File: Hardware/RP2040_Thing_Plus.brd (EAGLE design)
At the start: 22.9 x 58.4 mm, 67 parts, among them J5 USB Female Type C Connector, J6 MICRO-SD-SDIOPUSH-PUSH, Q1 2.5A/30V, U1 MCP73831, U2 MAX17048, U3 AP2112K-3.3V, U4 W25QXX128MBIT, U5 RP2040, Y2 12MHz

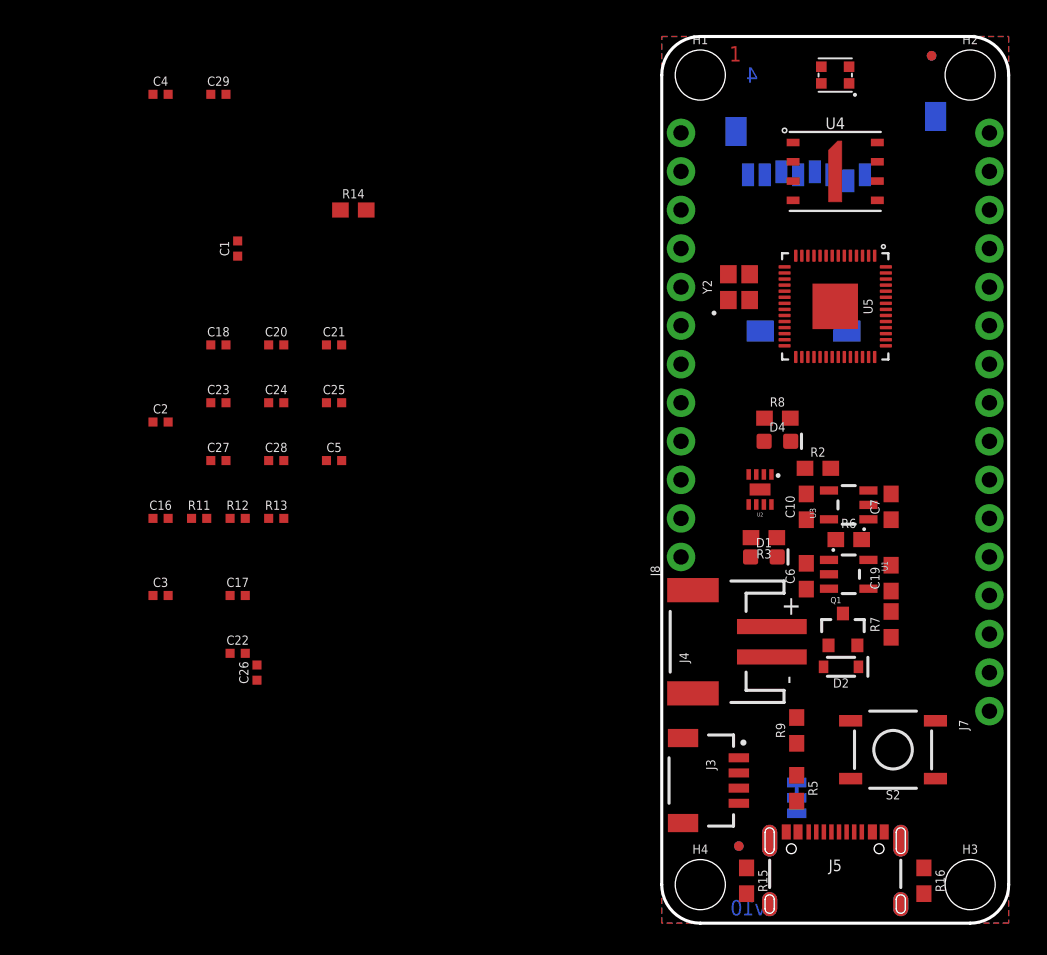
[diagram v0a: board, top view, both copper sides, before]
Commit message: airwire corrections
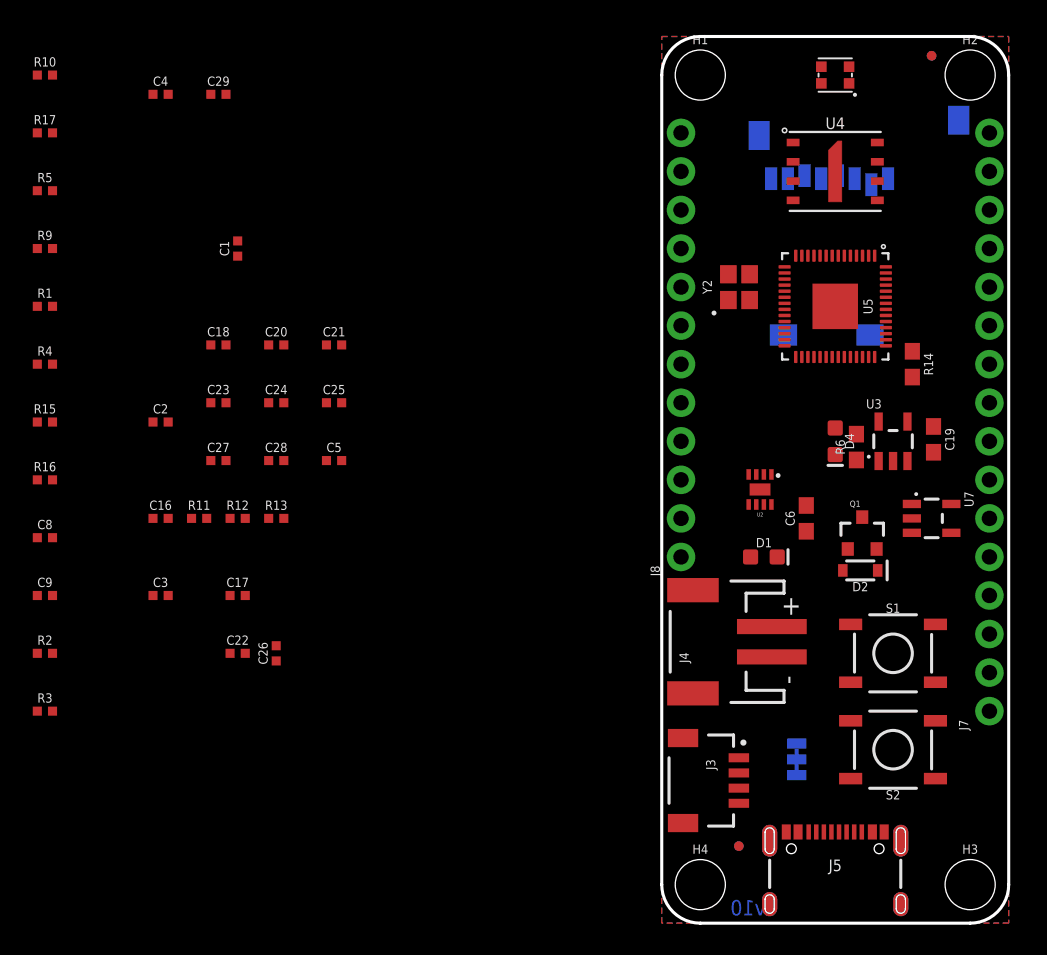
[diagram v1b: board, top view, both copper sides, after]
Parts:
- removed C10: 2.2uF, SparkFun-Capacitors:0603
- removed C7: 1.0uF, SparkFun-Capacitors:0603@1
- removed R7: 10k, SparkFun-Resistors:0603
- removed R8: 330, SparkFun-Resistors:0603
- removed U1: MCP73831, SparkFun-PowerIC:SOT23-5
- added C8: 1.0uF, SparkFun-Capacitors:0402-TIGHT
- added C9: 2.2uF, SparkFun-Capacitors:0402-TIGHT
- added R1, R4: 5.1k, SparkFun-Resistors:0402-TIGHT
- added R10, R17: 2.2k, SparkFun-Resistors:0402-TIGHT
- added S1: MOMENTARY-SWITCH-SPST-SMD-5.2MM-TALL, SparkFun-Switches:TACTILE_SWITCH_SMD_5.2MM
- added U7: 3.3V, SparkFun-IC-Power:SOT23-5
- C19, C6: device SparkFun-Capacitors:0603@1 -> SparkFun-Capacitors:0603
- J3: value (none) -> QWIIC_RIGHT_ANGLE
- R15, R16: value 5.1k -> 10k; device SparkFun-Resistors:0603 -> SparkFun-Resistors:0402-TIGHT
- R2: value 10k -> 1k; device SparkFun-Resistors:0603 -> SparkFun-Resistors:0402-TIGHT
- R3: value 1K -> 1k; device SparkFun-Resistors:0603 -> SparkFun-Resistors:0402-TIGHT
- R5: value 2.2k -> 1k; device SparkFun-Resistors:0603 -> SparkFun-Resistors:0402-TIGHT
- R9: value 2.2k -> 10k; device SparkFun-Resistors:0603 -> SparkFun-Resistors:0402-TIGHT
- U3: value AP2112K-3.3V -> MCP73831; device SparkFun-PowerIC:SOT23-5 -> SparkFun-IC-Power:SOT23-5
- moved R16 63.7 mm to (-40.6, 29.2), turned to 0 degrees
- moved R5 63.3 mm to (-40.6, 48.3), turned to 0 degrees
- moved R9 58.8 mm to (-40.6, 44.5), turned to 0 degrees
- moved R15 55.2 mm to (-40.6, 33.0), turned to 0 degrees
- moved R2 52.4 mm to (-40.6, 17.8)
- moved R3 48.7 mm to (-40.6, 14.0), turned to 0 degrees
- moved R14 38.2 mm to (16.5, 36.8), turned to 270 degrees
- moved C19 9.56 mm to (17.9, 31.9), turned to 270 degrees
- moved D2 6.48 mm to (13.1, 23.2)
- moved Q1 6.48 mm to (13.2, 25.7)
- moved R6 6.12 mm to (12.8, 31.4), turned to 90 degrees
- moved U3 5.11 mm to (15.2, 31.8), turned to 0 degrees
- moved C6 3.81 mm to (9.53, 26.7)
- moved D4 3.81 mm to (11.4, 31.8), turned to 270 degrees
- moved U$68 2.54 mm to (6.10, 11.6)
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- renumbered U$3 to U6
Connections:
- removed net D13: D4.A
- removed net VIN: C7.1, D2.C, Q1.2, R2.2, U3.1
- new net BOOT: R5.2, S1.3
- new net N$15: C8.1, D2.C, Q1.2, R16.2, U7.1
- net 3.3V: now also C9.1, R9.2, U7.5; no longer C10.1, U3.5
- net EN: now also R16.1, U7.3; no longer R2.1, U3.3
- net GND: now also C8.2, C9.2, R1.2, R15.1, R3.1, R4.2, S1.1, U7.2; no longer C10.2, C7.2, R15.2, R16.2, R7.1, R8.1, U1.2
- net I2C1_SCL: now also R10.1; no longer R5.1
- net I2C1_SDA: now also R17.1; no longer R9.1
- net LED_BUILTIN: now also D4.A
- net N$1: now also R3.2; no longer R8.2
- net N$11: now also R1.1; no longer R15.1
- net N$12: now also R4.1; no longer R16.1
- net N$14: now also U3.5; no longer U1.5
- net N$17: now also R2.1; no longer R3.2
- net N$2: now also R10.2; no longer R5.2
- net N$3: now also R17.2; no longer R9.2
- net N$9: now also U3.1; no longer U1.1
- net QSPI-CS: now also R5.1, R9.1
- net V_BATT: now also U3.3; no longer U1.3
- net V_USB: now also R15.2, R2.2, U3.4; no longer R3.1, R7.2, U1.4
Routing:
- net I2C1_SCL: track 35.2 -> 0.00 mm
- net I2C1_SDA: track 32.3 -> 0.00 mm
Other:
- board text removed: "1"
- board text removed: "2"
- board text removed: "3"
- board text removed: "4"

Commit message: v01 review
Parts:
- removed C19, C6: 4.7uF, SparkFun-Capacitors:0603
- removed R14: 200, SparkFun-Resistors:0603
- removed U$67: (no value), buzzard_labels (39):I_C0
- removed U$68: (no value), buzzard_labels (39):21
- added C10, C7: 4.7uF, SparkFun-Capacitors:0402-TIGHT
- added J1: CORTEX_JTAG_DEBUG_MINIMUM_PTH, SparkFun-Connectors:2X5-PTH-1.27MM
- added R7: 200OHM-0402T-1/16W-1%, SparkFun-Resistors:0402-TIGHT
- added U$1, U$39: (no value), output:#_16#0
- added U$10: (no value), output:#WS2812_#0
- added U$11: (no value), output:#0#TX_#0
- added U$12: (no value), output:#1#RX_#0
- added U$13: (no value), output:#4#CIPO_#0
- added U$14: (no value), output:#3#COPI_#0
- added U$15: (no value), output:#2#SCK_#0
- added U$16, U$17, U$51, U$52: (no value), output:#NC_#0
- added U$18, U$50: (no value), output:#29#ADC3_#0
- added U$19, U$49: (no value), output:#28#ADC2_#0
- added U$2, U$38: (no value), output:#_17#0
- added U$20, U$48: (no value), output:#27#ADC1_#0
- added U$21, U$47: (no value), output:#26#ADC0_#0
- added U$22, U$40: (no value), output:#_VUSB#0
- added U$23, U$41: (no value), output:#_EN#0
- added U$24, U$42: (no value), output:#_VBATT#0
- added U$25, U$46: (no value), output:#GND_#0
- added U$26, U$45: (no value), output:#AREF_#0
- added U$27, U$44: (no value), output:#3#3V_#0
- added U$28, U$43: (no value), output:##RESET##0
- added U$29, U$9: (no value), output:#_SDA#6#0
- added U$3, U$37: (no value), output:#_18#0
- added U$30: (no value), Labels:I_SUPER2_C-()-03
- added U$32: (no value), SparkFun-Aesthetics:SFE_LOGO_NAME_FLAME_.1
- added U$33, U$7: (no value), output:#_22#0
- added U$34, U$6: (no value), output:#_21#0
- added U$35, U$5: (no value), output:#_20#0
- added U$36, U$4: (no value), output:#_19#0
- added U$53: (no value), output:RP2040_THING_PLUS0
- added U$59: (no value), output:#BOOT#0
- added U$60: (no value), output:#WS2812#0
- added U$61: (no value), output:#25#0
- added U$62: (no value), output:#CHARGE#0
- added U$64: (no value), SparkFun-Aesthetics:QWIIC_4MM
- added U$8: (no value), output:#_SCL#7#23#0
- R6: value 2.0k -> 2.0KOHM-0402T-1/16W-5%; device SparkFun-Resistors:0603 -> SparkFun-Resistors:0402-TIGHT
- moved R10 68.7 mm to (8.26, 7.62), flipped to the bottom, turned to 180 degrees
- moved R4 66.5 mm to (16.9, 3.43), turned to 90 degrees
- moved R17 63.6 mm to (8.26, 11.4), flipped to the bottom, turned to 180 degrees
- moved R1 59.6 mm to (5.97, 3.56), turned to 90 degrees
- moved R5 59.5 mm to (15.6, 28.8), flipped to the bottom, turned to 180 degrees
- moved R9 58.2 mm to (15.6, 29.7), flipped to the bottom, turned to 180 degrees
- moved R15 58.0 mm to (14.2, 14.2), turned to 180 degrees
- moved C9 55.9 mm to (15.2, 22.6), turned to 180 degrees
- moved C3 54.1 mm to (11.4, 52.5)
- moved R16 53.7 mm to (12.3, 20.1), turned to 90 degrees
- moved C22 53.4 mm to (14.7, 49.9), turned to 90 degrees
- moved R3 53.4 mm to (9.02, 33.5), turned to 270 degrees
- moved C8 53.1 mm to (12.3, 22.1), turned to 90 degrees
- moved R2 52.6 mm to (10.8, 29.0)
- moved C18 48.6 mm to (19.1, 43.6)
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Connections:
- net N$7 renamed USB_F_N
- net N$8 renamed USB_F_P
- removed net D+: J5.A6, J5.B6
- removed net D-: J5.A7, J5.B7
- removed net I2C1_SCL: J3.4, J8.11, R10.1, U2.7, U5.9
- removed net N$10: C28.1, R14.1, U5.43
- removed net N$23: U5.11
- removed net USB_D+: R13.1
- removed net USB_D-: R12.1
- new net AVDD: C28.1, J7.3, R7.1, U5.43
- new net I2C1_SCL/GPIO23: J3.4, J8.11, R10.1, U2.7, U5.35, U5.9
- new net USB_N: J5.A7, J5.B7, R12.1
- new net USB_P: J5.A6, J5.B6, R13.1
- net !RESET: now also J1.10
- net 3.3V: now also J1.1, R7.2; no longer R14.2
- net BATT_ALERT: now also U5.36; no longer U5.7
- net GND: now also C10.2, C7.2, J1.3, J1.5, J1.9; no longer C19.2, C6.2
- net GPIO16: now also J8.4; no longer J8.10
- net GPIO17: now also J8.5; no longer J8.9
- net GPIO18: now also J8.6; no longer J8.8
- net GPIO20: now also J8.8; no longer J8.6
- net GPIO21: now also J8.9; no longer J8.5
- net GPIO22: now also J8.10; no longer J8.4
- net N$13: now also U5.7; no longer U5.35
- net SWDCK: now also J1.4
- net SWDIO: now also J1.2
- net V_BATT: now also C10.1; no longer C6.1
- net V_USB: now also C7.1; no longer C19.1
- net WS2812_DI: now also U5.11; no longer U5.36
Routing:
- net I2C1_SCL/GPIO23: track 0.00 -> 72.6 mm, vias 0 -> 5
- net I2C1_SDA: track 0.00 -> 70.1 mm, vias 0 -> 3
- net 3.3V: track 0.00 -> 53.5 mm, vias 0 -> 15
- net V_USB: track 0.00 -> 43.7 mm, vias 0 -> 4
- net QSPI-0: track 0.00 -> 36.0 mm, vias 0 -> 3
- net USB_N: track 0.00 -> 35.0 mm, vias 0 -> 1
- net V_BATT: track 0.00 -> 35.0 mm, vias 0 -> 2
- net USB_P: track 0.00 -> 34.9 mm, vias 0 -> 1
- net QSPI-3: track 0.00 -> 34.2 mm, vias 0 -> 3
- net QSPI-CLK: track 0.00 -> 34.0 mm, vias 0 -> 3
- net !RESET: track 0.00 -> 33.0 mm, vias 0 -> 1
- net AVDD: track 0.00 -> 30.5 mm, vias 0 -> 1
- net BOOT: track 0.00 -> 27.5 mm, vias 0 -> 3
- net 1.1V: track 0.00 -> 27.0 mm, vias 0 -> 2
- net QSPI-CS: track 0.00 -> 26.2 mm, vias 0 -> 2
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
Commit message: Review Changes
- Add "Pi Thing Plus RP2040" silk
- Align LEDs
- Change LED label style
- Flip bottom silk labels
- Add GND vias
- Beef up power traces
- Add thermal vias under RP2040
- Straighten trace on ADC0
- Add SDA/SCL Labels to bottom silk
- Add PWR LED
- Move QSPI resistors to make room for silk

Passes micromod.dru (overlap errors for jumper footprint + thermal vias)
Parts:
- removed U$46: (no value), output:#GND_#0
- removed U$47: (no value), output:#26#ADC0_#0
- removed U$48: (no value), output:#27#ADC1_#0
- removed U$49: (no value), output:#28#ADC2_#0
- removed U$50: (no value), output:#29#ADC3_#0
- removed U$51, U$52: (no value), output:#NC_#0
- removed U$53: (no value), output:RP2040_THING_PLUS0
- added D3: RED, SparkFun-LED:LED-0603
- added R8: 1k, SparkFun-Resistors:0402-TIGHT
- added U$54: (no value), output:250
- added U$55: (no value), output:CHARGE0
- added U$56: (no value), output:BOOT0
- added U$57: (no value), output:#22_#0
- added U$58: (no value), output:#21_#0
- added U$63: (no value), output:#17_#0
- added U$65: (no value), output:#16_#0
- added U$66: (no value), output:#VUSB_#0
- added U$67: (no value), output:#EN_#0
- added U$68: (no value), output:#VBATT_#0
- added U$69, U$70: (no value), output:#_NC#0
- U$16: device output:#NC_#0 -> output:PWR0
- U$17: device output:#NC_#0 -> output:#I�C#0
- U$29: device output:#_SDA#6#0 -> output:PI_THING_PLUS0
- U$30: device Labels:I_SUPER2_C-()-03 -> output:RP20400
- U$33: device output:#_22#0 -> output:#SCL_#0
- U$34: device output:#_21#0 -> output:#SDA_#0
- U$35: device output:#_20#0 -> output:#_#RESET##0
- U$36: device output:#_19#0 -> output:#_3#3V#0
- U$37: device output:#_18#0 -> output:#_AREF#0
- U$38: device output:#_17#0 -> output:#_GND#0
- U$39: device output:#_16#0 -> output:#_26#ADC0#0
- U$40: device output:#_VUSB#0 -> output:#_27#ADC1#0
- U$41: device output:#_EN#0 -> output:#_28#ADC2#0
- U$42: device output:#_VBATT#0 -> output:#_29#ADC3#0
- U$43: device output:##RESET##0 -> output:PI_THING_PLUS_0
- U$44: device output:#3#3V_#0 -> output:RP2040_0
- U$45: device output:#AREF_#0 -> SparkFun-Aesthetics:SFE_LOGO_NAME_.1
- U$59: device output:#BOOT#0 -> output:#20_#0
- U$61: device output:#25#0 -> output:#19_#0
- U$62: device output:#CHARGE#0 -> output:#18_#0
- moved U$35 34.2 mm to (21.2, 14.0), turned to 0 degrees
- moved U$29 34.0 mm to (8.08, 18.7), flipped to the bottom
- moved U$16 31.7 mm to (18.8, 5.21)
- moved U$36 30.2 mm to (21.2, 16.5), turned to 0 degrees
- moved U$59 29.5 mm to (1.65, 41.9), flipped to the bottom
- moved U$17 28.9 mm to (6.63, 9.53), flipped to the bottom, turned to 90 degrees
- moved U$37 26.5 mm to (21.2, 19.1), turned to 0 degrees
- moved U$38 23.4 mm to (21.2, 21.6), turned to 0 degrees
- moved U$43 21.8 mm to (16.5, 35.3), flipped to the top, turned to 0 degrees
- moved U$39 21.1 mm to (21.2, 24.1), turned to 0 degrees
- moved U$42 21.1 mm to (21.2, 31.8), turned to 0 degrees
- moved U$40 19.8 mm to (21.2, 26.7), turned to 0 degrees
- moved U$41 19.8 mm to (21.2, 29.2), turned to 0 degrees
- moved U$45 18.8 mm to (14.4, 36.6), flipped to the top, turned to 0 degrees
- moved U$44 18.3 mm to (16.6, 34.1), flipped to the top, turned to 0 degrees
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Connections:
- new net N$7: D3.C, R8.2
- net 3.3V: now also D3.A
- net GND: now also R8.1
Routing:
- net N$7: track 0.00 -> 2.43 mm
- net QSPI-CS: track 26.2 -> 24.6 mm
- net BOOT: track 27.5 -> 28.8 mm
- net UART0_RX: track 9.54 -> 10.7 mm
- net V_BATT: track 35.0 -> 35.6 mm
- net N$15: track 9.41 -> 9.95 mm
- net 3.3V: track 53.5 -> 52.9 mm, vias 15 -> 16
- net GND: vias 9 -> 50
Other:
- board text added: "N. Poole"

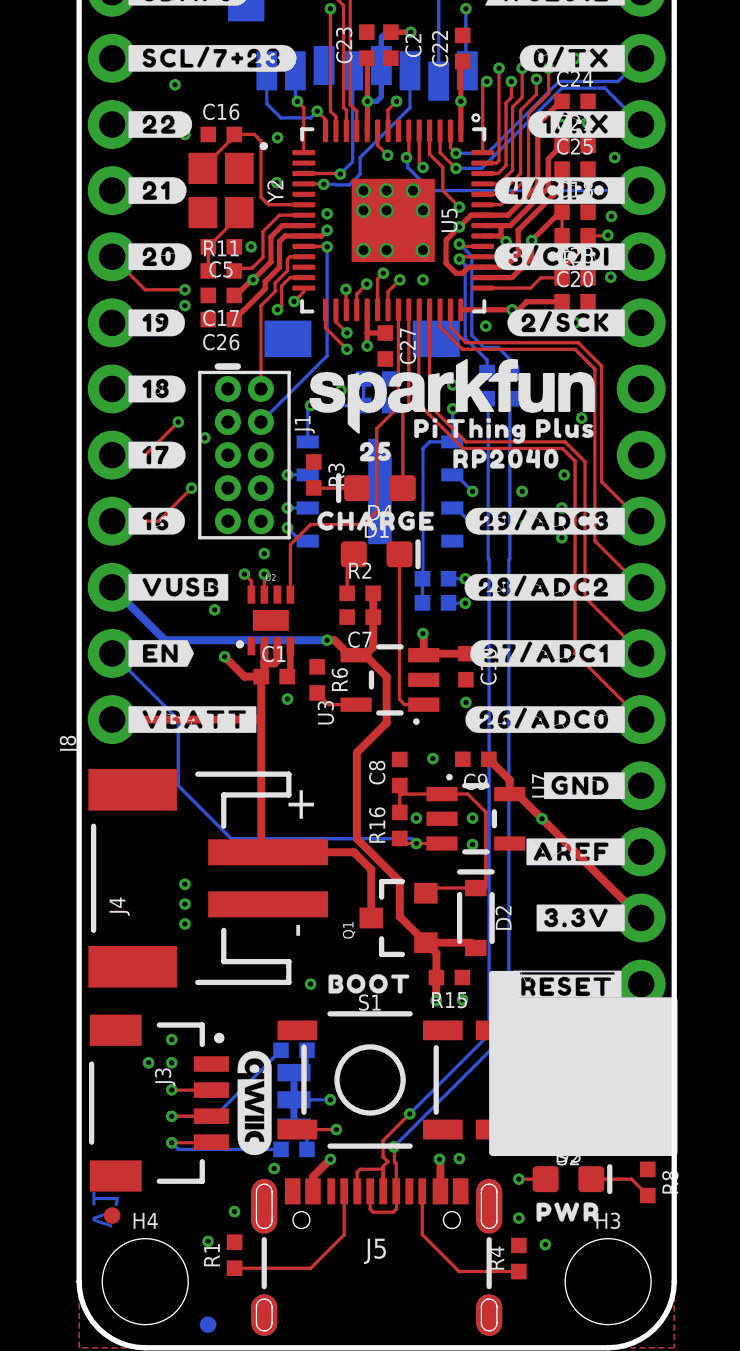
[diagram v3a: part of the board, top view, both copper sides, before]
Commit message: Move silk on LiPo connector. Add ignore. Remove backups.
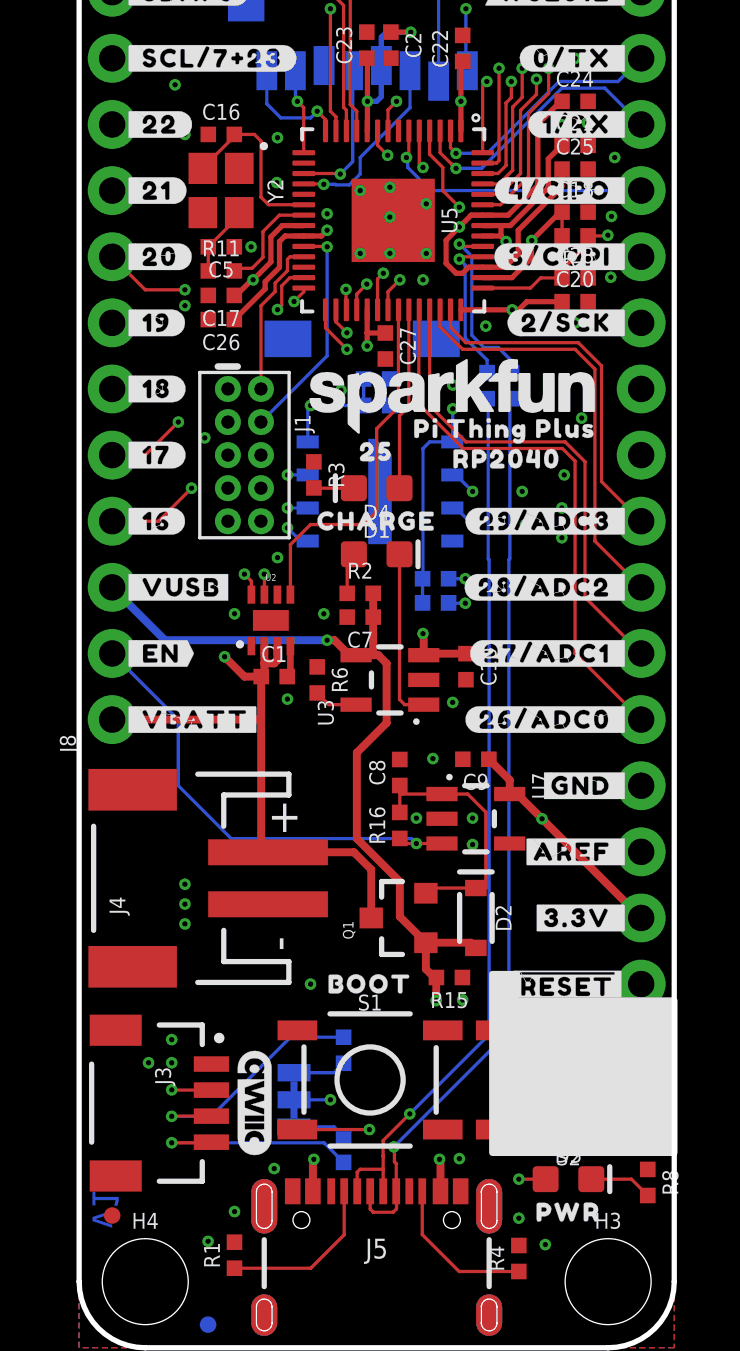
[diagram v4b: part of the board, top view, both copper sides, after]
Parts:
- moved U$32 35.9 mm to (8.89, 18.4)
- moved U$30 3.01 mm to (8.89, 14.0)
- moved U$29 2.81 mm to (8.89, 16.0)
- moved R10 1.90 mm to (10.2, 7.62), turned to 90 degrees
- moved R17 1.90 mm to (10.2, 11.4), turned to 270 degrees
- moved D4 0.13 mm to (11.4, 33.0)
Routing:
- net I2C1_SDA: track 70.1 -> 72.7 mm
- net I2C1_SCL/GPIO23: track 72.6 -> 75.2 mm
- net N$2: track 1.24 -> 2.66 mm
- net USB_N: track 34.9 -> 33.9 mm
- net N$3: track 1.24 -> 2.06 mm
- net V_USB: track 43.7 -> 44.5 mm
- net GND: vias 50 -> 49
